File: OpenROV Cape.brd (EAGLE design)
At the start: 71.8 x 54.6 mm, 26 parts, among them T1 2N2222, T2 TIP122

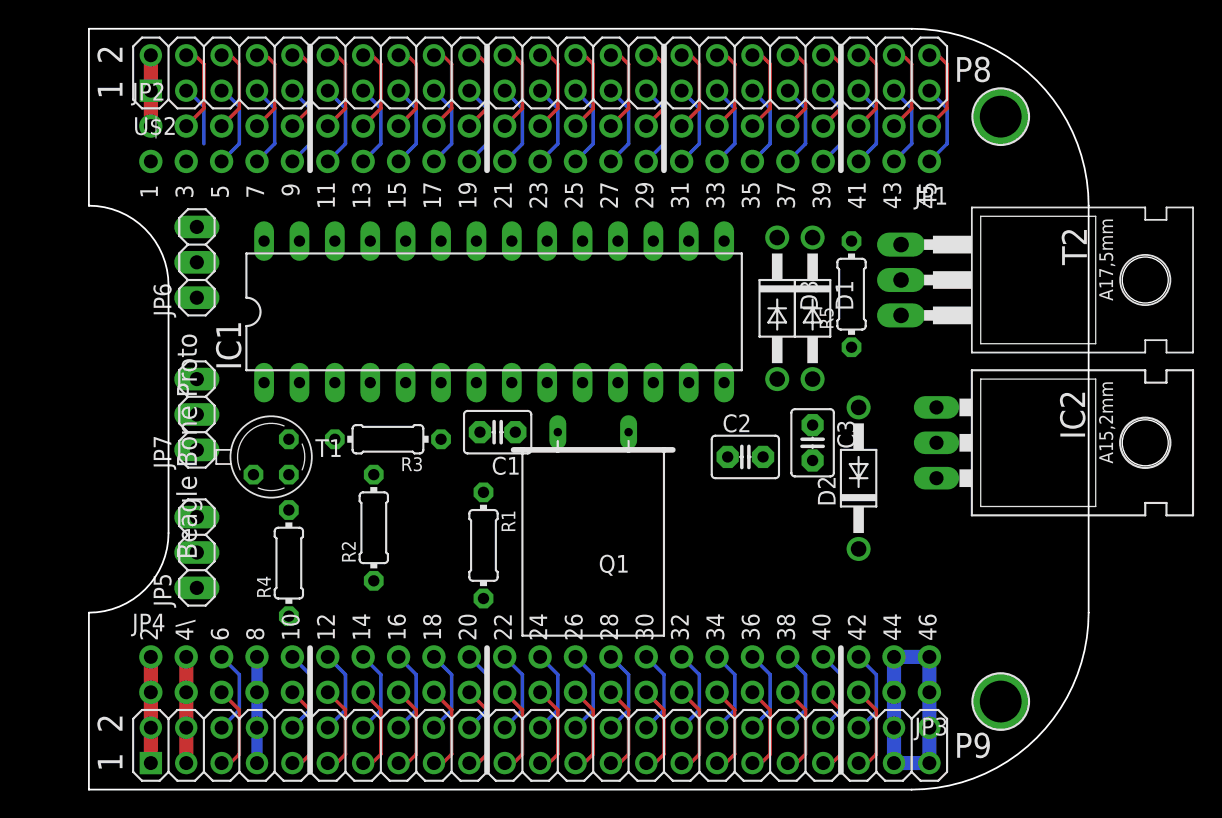
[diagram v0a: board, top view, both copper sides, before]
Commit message: removed the extra beagle board header pins to make more room for arduino pins
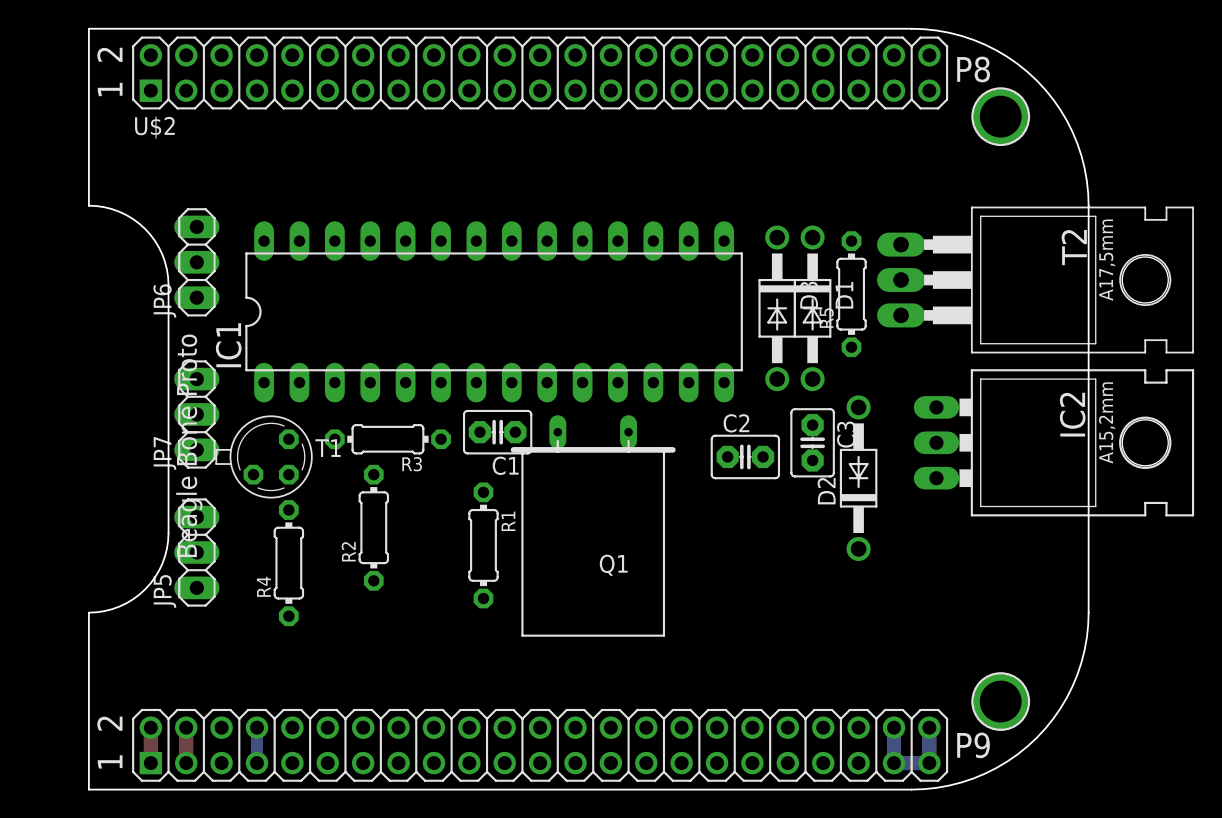
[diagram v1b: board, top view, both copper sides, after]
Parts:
- removed JP1, JP2, JP3, JP4: (no value), microbuilder:1X23_ROUND_70MIL
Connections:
- removed net N$10: JP1.14, U$2.19
- removed net N$11: JP1.13, U$2.21
- removed net N$12: JP1.12, U$2.23
- removed net N$13: JP1.11, U$2.25
- removed net N$14: JP1.10, U$2.27
- removed net N$15: JP1.9, U$2.29
- removed net N$16: JP1.8, U$2.31
- removed net N$17: JP1.7, U$2.33
- removed net N$18: JP1.6, U$2.35
- removed net N$19: JP1.5, U$2.37
- removed net N$21: JP1.3, U$2.41
- removed net N$22: JP1.2, U$2.43
- removed net N$23: JP1.1, U$2.45
- removed net N$27: JP2.4, U$2.8
- removed net N$28: JP2.5, U$2.10
- removed net N$29: JP2.6, U$2.12
- removed net N$30: JP2.7, U$2.14
- removed net N$31: JP2.8, U$2.16
- removed net N$32: JP2.9, U$2.18
- removed net N$33: JP2.10, U$2.20
- removed net N$34: JP2.11, U$2.22
- removed net N$35: JP2.12, U$2.24
- removed net N$36: JP2.13, U$2.26
- removed net N$37: JP2.14, U$2.28
- removed net N$38: JP2.15, U$2.30
- removed net N$39: JP2.16, U$2.32
- removed net N$4: JP1.20, U$2.7
- removed net N$40: JP2.17, U$2.34
- removed net N$41: JP2.18, U$2.36
- removed net N$43: JP2.20, U$2.40
- removed net N$44: JP2.21, U$2.42
- removed net N$45: JP2.22, U$2.44
- removed net N$47: JP1.22, U$2.3
- removed net N$48: JP1.21, U$2.5
- removed net N$49: JP3.21, U$2.51
- removed net N$5: JP1.19, U$2.9
- removed net N$50: JP2.2, U$2.4
- removed net N$51: JP3.19, U$2.55
- removed net N$52: JP3.18, U$2.57
- removed net N$53: JP3.17, U$2.59
- removed net N$54: JP3.16, U$2.61
- removed net N$55: JP3.15, U$2.63
- removed net N$56: JP3.14, U$2.65
- removed net N$57: JP3.13, U$2.67
- removed net N$58: JP3.12, U$2.69
- removed net N$59: JP3.11, U$2.71
- removed net N$6: JP1.18, U$2.11
- removed net N$60: JP3.10, U$2.73
- removed net N$61: JP3.9, U$2.75
- removed net N$62: JP3.8, U$2.77
- removed net N$63: JP3.7, U$2.79
- removed net N$64: JP3.6, U$2.81
- removed net N$65: JP3.5, U$2.83
- removed net N$66: JP3.4, U$2.85
- removed net N$67: JP3.3, U$2.87
- removed net N$68: JP2.3, U$2.6
- removed net N$69: JP4.21, U$2.88
- removed net N$7: JP1.17, U$2.13
- removed net N$72: JP4.3, U$2.52
- removed net N$74: JP4.5, U$2.56
- removed net N$75: JP4.6, U$2.58
- removed net N$76: JP4.7, U$2.60
- removed net N$77: JP4.8, U$2.62
- removed net N$78: JP4.9, U$2.64
- removed net N$79: JP4.10, U$2.66
- removed net N$8: JP1.16, U$2.15
- removed net N$80: JP4.11, U$2.68
- removed net N$81: JP4.12, U$2.70
- removed net N$82: JP4.13, U$2.72
- removed net N$83: JP4.14, U$2.74
- removed net N$84: JP4.15, U$2.76
- removed net N$85: JP4.16, U$2.78
- removed net N$86: JP4.17, U$2.80
- removed net N$87: JP4.18, U$2.82
- removed net N$88: JP4.19, U$2.84
- removed net N$89: JP4.20, U$2.86
- removed net N$9: JP1.15, U$2.17
- new net AIN0: U$2.85
- new net AIN3: U$2.84
- new net GPIO1_6: U$2.3
- new net GPIO1_7: U$2.4
- new net GPIO2_11: U$2.42
- new net GPIO2_6: U$2.45
- new net GPIO2_8: U$2.43
- new net GPIO2_9: U$2.44
- new net VDD_5V: U$2.51, U$2.52
- net 3.3V: no longer JP3.22, JP4.2
- net 5.0V: no longer JP3.20, JP4.4
- net AGND: no longer JP2.19
- net AVCC: no longer JP1.4
- net GND: no longer JP1.23, JP2.1, JP3.1, JP3.2, JP3.23, JP4.1, JP4.22, JP4.23
- net N$46: no longer JP2.23
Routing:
- net GND: track 33.0 -> 10.2 mm
- net N$67: track 6.50 -> 0.00 mm
- net N$65: track 6.50 -> 0.00 mm
- net N$44: track 6.50 -> 0.00 mm
- net AGND: track 6.50 -> 0.00 mm
- net N$64: track 6.50 -> 0.00 mm
- net N$63: track 6.50 -> 0.00 mm
- net N$56: track 6.50 -> 0.00 mm
- net N$55: track 6.50 -> 0.00 mm
- net N$54: track 6.50 -> 0.00 mm
- net N$62: track 6.50 -> 0.00 mm
- net N$61: track 6.50 -> 0.00 mm
- net N$60: track 6.50 -> 0.00 mm
- net N$53: track 6.50 -> 0.00 mm
- net N$52: track 6.50 -> 0.00 mm
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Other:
- board text removed: "10"
- board text removed: "11"
- board text removed: "12"
- board text removed: "13"
- board text removed: "14"
- board text removed: "15"
- board text removed: "16"
- board text removed: "17"
- board text removed: "18"
- board text removed: "19"
- board text removed: "20"
- board text removed: "21"
- board text removed: "22"
- board text removed: "23"
- board text removed: "24"
- board text removed: "25"
- board text removed: "26"
- board text removed: "27"
- board text removed: "28"
- board text removed: "29"
- board text removed: "3"
- board text removed: "30"
- board text removed: "31"
- board text removed: "32"
- board text removed: "33"
- board text removed: "34"
- board text removed: "35"
- board text removed: "36"
- board text removed: "37"
- board text removed: "38"
- board text removed: "39"
- board text removed: "40"
- board text removed: "41"
- board text removed: "42"
- board text removed: "43"
- board text removed: "44"
- board text removed: "45"
- board text removed: "46"
- board text removed: "4\"
- board text removed: "5"
- board text removed: "6"
- board text removed: "7"
- board text removed: "8"
- board text removed: "9"

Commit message: swapped out IC1 for official sparkfun atmega328 footprint
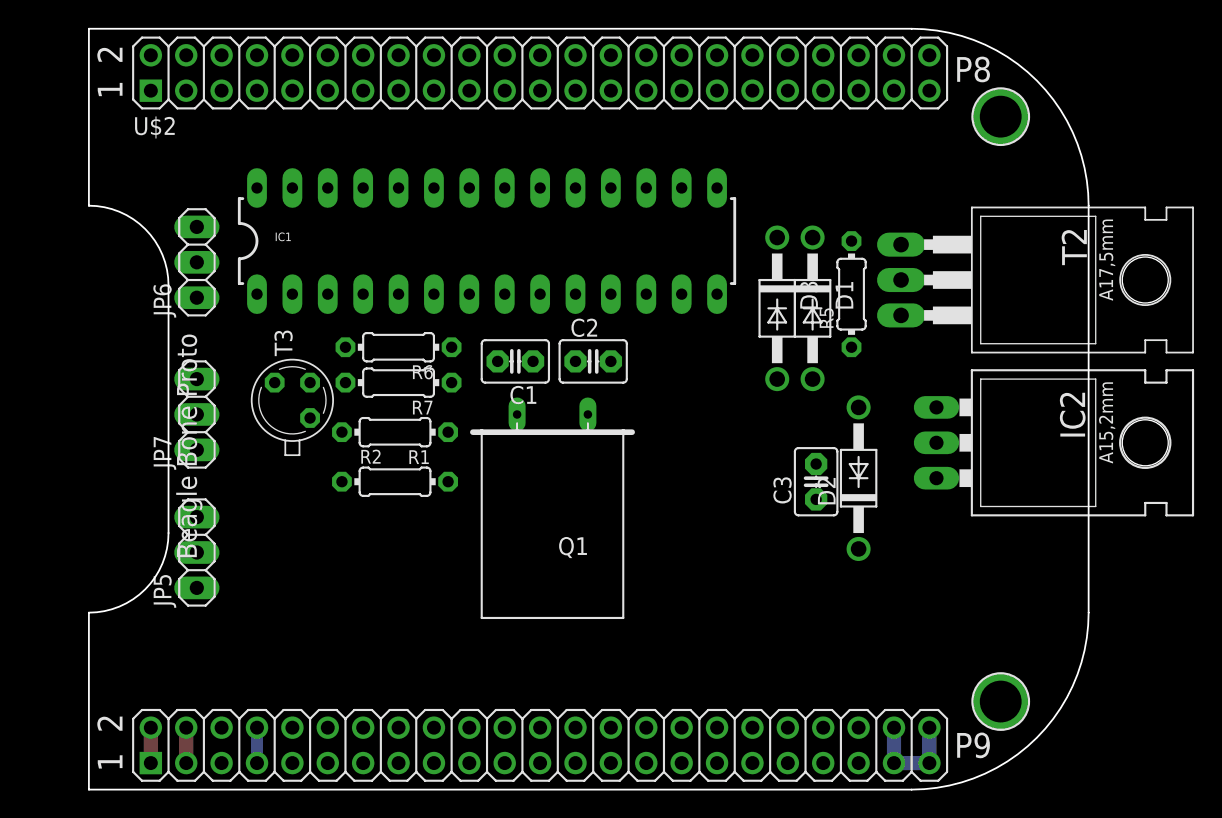
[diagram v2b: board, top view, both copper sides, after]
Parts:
- removed R3, R4: (no value), rcl:0204/7
- removed T1: 2N2222, transistor:TO18
- added R6, R7: (no value), rcl:0204/7
- added T3: 2N2222, transistor:TO18
- IC1: value (none) -> ATMEGA328P-PU; device ic-package:DIL28-4 -> SparkFun:DIL28-3
- moved C2 12.9 mm to (50.8, 30.7)
- moved R1 10.3 mm to (36.6, 25.7), turned to 180 degrees
- moved C1 5.24 mm to (45.2, 30.7)
- moved IC1 5.11 mm to (43.2, 39.4)
- moved R2 3.64 mm to (36.6, 22.1), turned to 0 degrees
- moved Q1 3.19 mm to (47.9, 19.3)
- moved C3 2.81 mm to (66.8, 22.1), turned to 90 degrees
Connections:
- removed net N$20: R4.1
- removed net N$26: IC1.15
- removed net N$3: R4.2, T1.2
- removed net N$42: IC1.16
- removed net N$70: IC1.17
- removed net N$96: IC1.3, R2.2
- new net N$4: IC1.1, R6.2, T3.3
- new net N$5: R7.2, T3.2
- new net N$6: R7.1
- net GND: now also T3.1; no longer IC1.22, IC1.8, T1.1
- net N$2: now also R2.2; no longer IC1.1, R3.2, T1.3
- net VCC: now also R6.1; no longer R3.1
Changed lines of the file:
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@@
 <element name="U$22" library="microbuilder" package="MOUNTINGHOLE_3.0_PLATEDTHIN" value="MOUNTINGHOLE3.0THIN" x="80.05" y="48.3"/>
 <element name="U$23" library="microbuilder" package="MOUNTINGHOLE_3.0_PLATEDTHIN" value="MOUNTINGHOLE3.0THIN" x="80.05" y="6.32"/>
-<element name="IC1" library="ic-package" package="DIL28-4" value="" x="43.688" y="34.29"/>
-<element name="R1" library="rcl" package="0204/7" value="" x="42.926" y="17.526" rot="R270"/>
-<element name="R2" library="rcl" package="0204/7" value="" x="35.052" y="18.796" rot="R90"/>
-<element name="R3" library="rcl" package="0204/7" value="" x="36.068" y="25.146" rot="R180"/>
-<element name="T1" library="transistor" package="TO18" value="2N2222" x="27.686" y="23.876"/>
-<element name="Q1" library="special" package="Q" value="" x="50.8" y="18.034" rot="R180"/>
-<element name="R4" library="rcl" package="0204/7" value="" x="28.956" y="16.256" rot="R90"/>
-<element name="C1" library="capacitor-wima" package="C2.5-3" value="" x="43.942" y="25.654" rot="R180"/>
-<element name="C2" library="capacitor-wima" package="C2.5-3" value="" x="61.722" y="23.876"/>
+<element name="R1" library="rcl" package="0204/7" value="" x="36.576" y="25.654" rot="R180"/>
+<element name="R2" library="rcl" package="0204/7" value="" x="36.576" y="22.098"/>
+<element name="Q1" library="special" package="Q" value="" x="47.879" y="19.304" rot="R180"/>
+<element name="C1" library="capacitor-wima" package="C2.5-3" value="" x="45.212" y="30.734" rot="R180"/>
+<element name="C2" library="capacitor-wima" package="C2.5-3" value="" x="50.8" y="30.734"/>
 <element name="D1" library="diode" package="DO41-10" value="1N4004" x="66.548" y="34.544" rot="R270"/>
 <element name="D2" library="diode" package="DO41-10" value="1N4004" x="69.85" y="22.352" rot="R90"/>
 <element name="R5" library="rcl" package="0204/7" value="" x="69.342" y="35.56" rot="R90"/>
 <element name="T2" library="transistor" package="TO220" value="TIP122" x="79.248" y="36.576" rot="R270"/>
-<element name="C3" library="capacitor-wima" package="C2.5-3" value="" x="66.548" y="24.892" rot="R270"/>
+<element name="C3" library="capacitor-wima" package="C2.5-3" value="" x="66.802" y="22.098" rot="R90"/>
 <element name="D3" library="diode" package="DO41-10" value="1N4004" x="64.008" y="34.544" rot="R270"/>
 <element name="IC2" library="v-reg" package="78XXL" value="" x="79.248" y="24.892" rot="R270"/>
@@
 <element name="JP6" library="pinhead" package="1X03" value="" x="22.352" y="37.846" rot="R90"/>
 <element name="JP7" library="pinhead" package="1X03" value="" x="22.352" y="26.924" rot="R90"/>
+<element name="IC1" library="SparkFun" package="DIL28-3" value="ATMEGA328P-PU" x="43.18" y="39.37"/>
+<element name="R6" library="rcl" package="0204/7" value="" x="36.83" y="31.75" rot="R180"/>
+<element name="T3" library="transistor" package="TO18" value="2N2222" x="29.21" y="27.94" rot="R90"/>
+<element name="R7" library="rcl" package="0204/7" value="" x="36.83" y="29.21" rot="R180"/>
 </elements>
 <signals>
@@
 <wire x1="72.39" y1="4.445" x2="72.39" y2="1.905" width="1.016" layer="16"/>
 <wire x1="72.39" y1="1.905" x2="74.93" y2="1.905" width="1.016" layer="16"/>
-<contactref element="IC1" pad="8"/>
-<contactref element="IC1" pad="22"/>
 <contactref element="R1" pad="1"/>
-<contactref element="T1" pad="1"/>
 <contactref element="C2" pad="2"/>
 <contactref element="C1" pad="2"/>
@@
 <contactref element="JP7" pad="3"/>
 <contactref element="U$2" pad="1"/>
-<wire x1="66.548" y1="23.622" x2="75.438" y2="24.892" width="0" layer="19" extent="1-1"/>
-<wire x1="62.992" y1="23.876" x2="66.548" y2="23.622" width="0" layer="19" extent="1-1"/>
-<wire x1="44.958" y1="29.21" x2="62.992" y2="23.876" width="0" layer="19" extent="1-1"/>
-<wire x1="42.672" y1="25.654" x2="44.958" y2="29.21" width="0" layer="19" extent="1-1"/>
-<wire x1="42.926" y1="21.336" x2="42.672" y2="25.654" width="0" layer="19" extent="1-1"/>
-<wire x1="42.418" y1="39.37" x2="44.958" y2="29.21" width="0" layer="19" extent="1-1"/>
-<wire x1="26.416" y1="22.606" x2="42.672" y2="25.654" width="0" layer="19" extent="1-1"/>
-<wire x1="22.352" y1="19.558" x2="26.416" y2="22.606" width="0" layer="19" extent="1-1"/>
-<wire x1="22.352" y1="29.464" x2="26.416" y2="22.606" width="0" layer="19" extent="1-1"/>
+<contactref element="T3" pad="1"/>
+<wire x1="66.802" y1="23.368" x2="75.438" y2="24.892" width="0" layer="19" extent="1-1"/>
+<wire x1="52.07" y1="30.734" x2="66.802" y2="23.368" width="0" layer="19" extent="1-1"/>
+<wire x1="72.39" y1="4.445" x2="66.802" y2="23.368" width="0" layer="19" extent="1-1"/>
+<wire x1="40.386" y1="25.654" x2="52.07" y2="30.734" width="0" layer="19" extent="1-1"/>
+<wire x1="43.942" y1="30.734" x2="40.386" y2="25.654" width="0" layer="19" extent="1-1"/>
+<wire x1="22.352" y1="19.558" x2="40.386" y2="25.654" width="0" layer="19" extent="1-1"/>
+<wire x1="22.352" y1="29.464" x2="22.352" y2="19.558" width="0" layer="19" extent="1-1"/>
 <wire x1="22.352" y1="40.386" x2="22.352" y2="29.464" width="0" layer="19" extent="1-1"/>
 <wire x1="19.05" y1="50.165" x2="22.352" y2="40.386" width="0" layer="19" extent="1-1"/>
 <wire x1="19.05" y1="52.705" x2="19.05" y2="50.165" width="0" layer="19" extent="1-1"/>
 <wire x1="19.05" y1="4.445" x2="22.352" y2="19.558" width="0" layer="19" extent="1-1"/>
-<wire x1="72.39" y1="4.445" x2="66.548" y2="23.622" width="0" layer="19" extent="1-1"/>
-</signal>
-<signal name="N$1">
-<contactref element="IC1" pad="2"/>
-</signal>
-<signal name="N$2">
-<contactref element="R3" pad="2"/>
-<contactref element="T1" pad="3"/>
-<contactref element="IC1" pad="1"/>
-<wire x1="28.956" y1="25.146" x2="32.258" y2="25.146" width="0" layer="19" extent="1-1"/>
-<wire x1="27.178" y1="29.21" x2="28.956" y2="25.146" width="0" layer="19" extent="1-1"/>
-</signal>
-<signal name="N$3">
-<contactref element="T1" pad="2"/>
-<contactref element="R4" pad="2"/>
-<wire x1="28.956" y1="20.066" x2="28.956" y2="22.606" width="0" layer="19" extent="1-1"/>
-</signal>
-<signal name="N$20">
-<contactref element="R4" pad="1"/>
+<wire x1="30.48" y1="26.67" x2="19.05" y2="1.905" width="0" layer="19" extent="1-1"/>
 </signal>
 <signal name="N$24">
-<contactref element="IC1" pad="10"/>
 <contactref element="Q1" pad="1"/>
 <contactref element="C2" pad="1"/>
-<wire x1="53.34" y1="25.654" x2="60.452" y2="23.876" width="0" layer="19" extent="1-1"/>
-<wire x1="50.038" y1="29.21" x2="53.34" y2="25.654" width="0" layer="19" extent="1-1"/>
+<contactref element="IC1" pad="10"/>
+<wire x1="49.53" y1="30.734" x2="49.53" y2="35.56" width="0" layer="19" extent="1-1"/>
+<wire x1="50.419" y1="26.924" x2="49.53" y2="30.734" width="0" layer="19" extent="1-1"/>
 </signal>
 <signal name="N$25">
 <contactref element="Q1" pad="2"/>
+<contactref element="C1" pad="1"/>
 <contactref element="IC1" pad="9"/>
-<contactref element="C1" pad="1"/>
-<wire x1="45.212" y1="25.654" x2="48.26" y2="25.654" width="0" layer="19" extent="1-1"/>
-<wire x1="47.498" y1="29.21" x2="48.26" y2="25.654" width="0" layer="19" extent="1-1"/>
-</signal>
-<signal name="N$26">
-<contactref element="IC1" pad="15"/>
-</signal>
-<signal name="N$42">
-<contactref element="IC1" pad="16"/>
-</signal>
-<signal name="N$70">
-<contactref element="IC1" pad="17"/>
+<wire x1="46.482" y1="30.734" x2="46.99" y2="35.56" width="0" layer="19" extent="1-1"/>
+<wire x1="45.339" y1="26.924" x2="46.482" y2="30.734" width="0" layer="19" extent="1-1"/>
 </signal>
 <signal name="N$71">
@@
 <contactref element="C3" pad="1"/>
 <contactref element="R5" pad="1"/>
-<wire x1="66.548" y1="26.162" x2="69.342" y2="31.75" width="0" layer="19" extent="1-1"/>
-<wire x1="69.85" y1="17.272" x2="66.548" y2="26.162" width="0" layer="19" extent="1-1"/>
+<wire x1="66.802" y1="20.828" x2="69.342" y2="31.75" width="0" layer="19" extent="1-1"/>
+<wire x1="69.85" y1="17.272" x2="66.802" y2="20.828" width="0" layer="19" extent="1-1"/>
 </signal>
 <signal name="N$73">
@@
 </signal>
 <signal name="VCC">
-<contactref element="R3" pad="1"/>
+<contactref element="IC2" pad="OUT"/>
+<contactref element="R6" pad="1"/>
 <contactref element="IC1" pad="7"/>
-<contactref element="IC2" pad="OUT"/>
-<wire x1="42.418" y1="29.21" x2="75.438" y2="22.352" width="0" layer="19" extent="1-1"/>
-<wire x1="39.878" y1="25.146" x2="42.418" y2="29.21" width="0" layer="19" extent="1-1"/>
+<wire x1="41.91" y1="35.56" x2="75.438" y2="22.352" width="0" layer="19" extent="1-1"/>
+<wire x1="40.64" y1="31.75" x2="41.91" y2="35.56" width="0" layer="19" extent="1-1"/>
 </signal>
 <signal name="N$92">
@@
 <contactref element="R1" pad="2"/>
 <contactref element="R2" pad="1"/>
-<wire x1="35.052" y1="14.986" x2="42.926" y2="13.716" width="0" layer="19" extent="1-1"/>
-</signal>
-<signal name="N$96">
-<contactref element="R2" pad="2"/>
-<contactref element="IC1" pad="3"/>
-<wire x1="35.052" y1="22.606" x2="32.258" y2="29.21" width="0" layer="19" extent="1-1"/>
+<wire x1="32.766" y1="22.098" x2="32.766" y2="25.654" width="0" layer="19" extent="1-1"/>
 </signal>
 <signal name="GPIO1_6">
@@
 <contactref element="U$2" pad="85"/>
 </signal>
+<signal name="N$4">
+<contactref element="R6" pad="2"/>
+<contactref element="T3" pad="3"/>
+<contactref element="IC1" pad="1"/>
+<wire x1="27.94" y1="29.21" x2="33.02" y2="31.75" width="0" layer="19" extent="1-1"/>
+<wire x1="26.67" y1="35.56" x2="27.94" y2="29.21" width="0" layer="19" extent="1-1"/>
+</signal>
+<signal name="N$5">
+<contactref element="T3" pad="2"/>
+<contactref element="R7" pad="2"/>
+<wire x1="30.48" y1="29.21" x2="33.02" y2="29.21" width="0" layer="19" extent="1-1"/>
+</signal>
+<signal name="N$6">
+<contactref element="R7" pad="1"/>
+</signal>
+<signal name="N$1">
+<contactref element="IC1" pad="2"/>
+</signal>
+<signal name="N$2">
+<contactref element="R2" pad="2"/>
+</signal>
 </signals>
